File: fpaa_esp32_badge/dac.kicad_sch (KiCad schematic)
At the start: 16 parts, among them J10 AudioPlug3, J23 Conn_01x02, U11 PCM5102

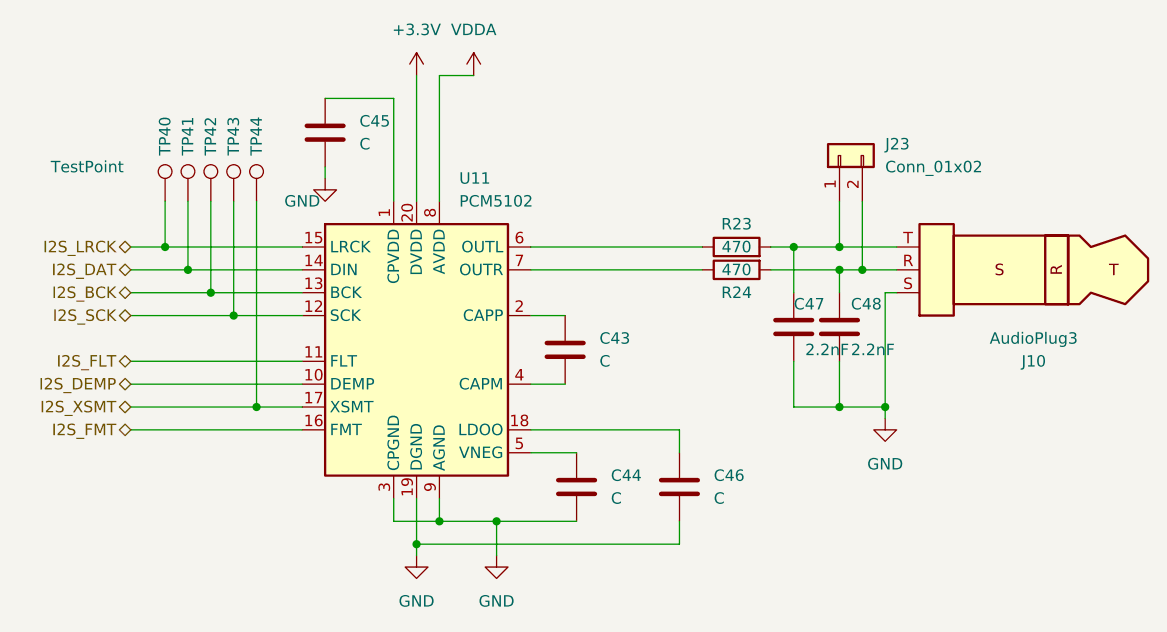
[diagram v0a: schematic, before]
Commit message: added pdf and corrected some part values
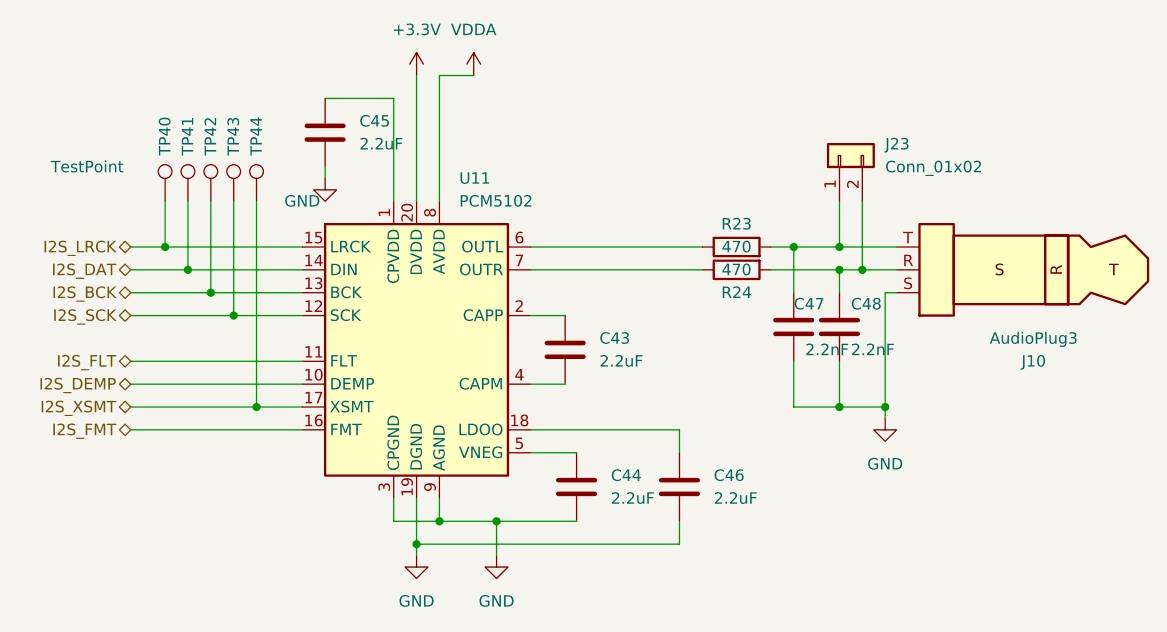
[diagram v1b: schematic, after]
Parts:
- C43, C44, C45, C46: value C -> 2.2uF
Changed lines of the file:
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@@
       (effects (font (size 1.27 1.27)) (justify left))
     )
-    (property "Value" "C" (at 130.81 59.69 0)
+    (property "Value" "2.2uF" (at 130.81 59.69 0)
       (effects (font (size 1.27 1.27)) (justify left))
     )
@@
       (effects (font (size 1.27 1.27)) (justify left))
     )
-    (property "Value" "C" (at 158.75 99.06 0)
+    (property "Value" "2.2uF" (at 158.75 99.06 0)
       (effects (font (size 1.27 1.27)) (justify left))
     )
@@
       (effects (font (size 1.27 1.27)) (justify left))
     )
-    (property "Value" "C" (at 157.48 83.82 0)
+    (property "Value" "2.2uF" (at 157.48 83.82 0)
       (effects (font (size 1.27 1.27)) (justify left))
     )
@@
       (effects (font (size 1.27 1.27)) (justify left))
     )
-    (property "Value" "C" (at 170.18 99.06 0)
-      (effects (font (size 1.27 1.27)) (justify left))
-    )
+    (property "Value" "2.2uF" (at 170.18 99.06 0)
+      (effects (font (size 1.27 1.27)) (justify left))
+    )
